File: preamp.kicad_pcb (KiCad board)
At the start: 2 copper layers, 49.5 x 43.2 mm, 46 parts, among them P1 CONN_01X04, P2 CONN_01X02, P3 CONN_01X04, P4 CONN_01X01, T1 TRANSFO2, U1 OPA137N, U2 LM7815CT, U3 LM7915CT, U4 OPA137N

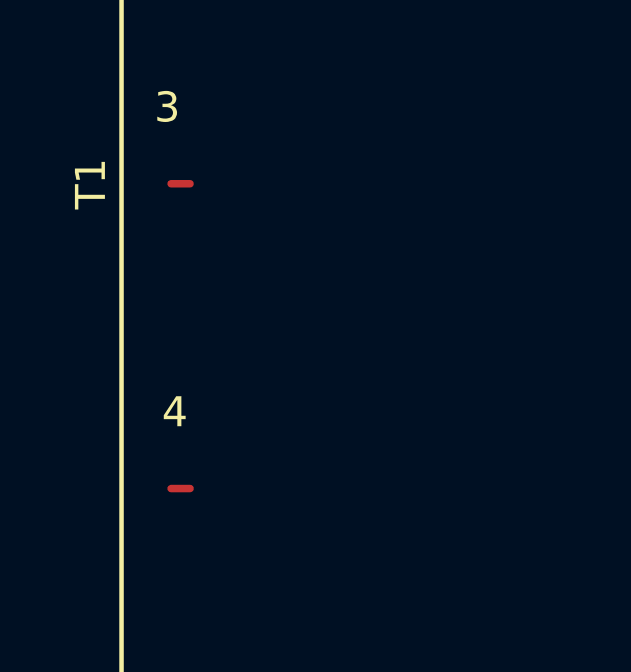
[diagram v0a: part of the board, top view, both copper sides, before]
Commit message: Clean up a couple of stray traces.
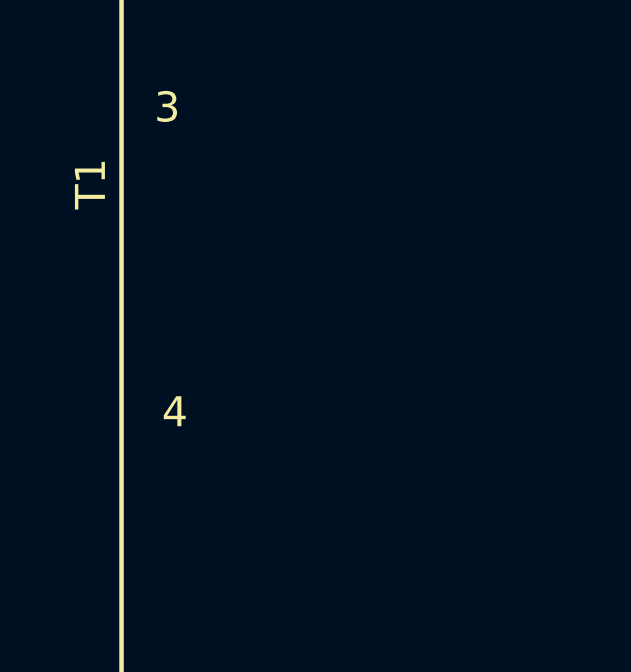
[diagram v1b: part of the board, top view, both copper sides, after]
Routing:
- net (no net): track 2.52 -> 1.25 mm
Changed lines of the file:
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@@
     (thickness 1.6)
     (drawings 9)
-    (tracks 232)
+    (tracks 230)
     (zones 0)
     (modules 46)
@@
   (page A4)
   (layers
-    (0 F.Cu signal hide)
+    (0 F.Cu signal)
     (31 B.Cu signal)
     (32 B.Adhes user)
@@
     (effects (font (size 0.5 0.5) (thickness 0.1)))
   )
-  (segment (start 42.038 78.74) (end 42.672 78.74) (width 0.25) (layer F.Cu) (net 0))
-  (segment (start 42.038 88.9) (end 42.672 88.9) (width 0.25) (layer F.Cu) (net 0))
   (segment (start 86.995 70.485) (end 87.138 70.628) (width 0.25) (layer F.Cu) (net 0))
   (segment (start 88.535 72.279) (end 88.535 71.755) (width 0.25) (layer F.Cu) (net 0) (status 30))

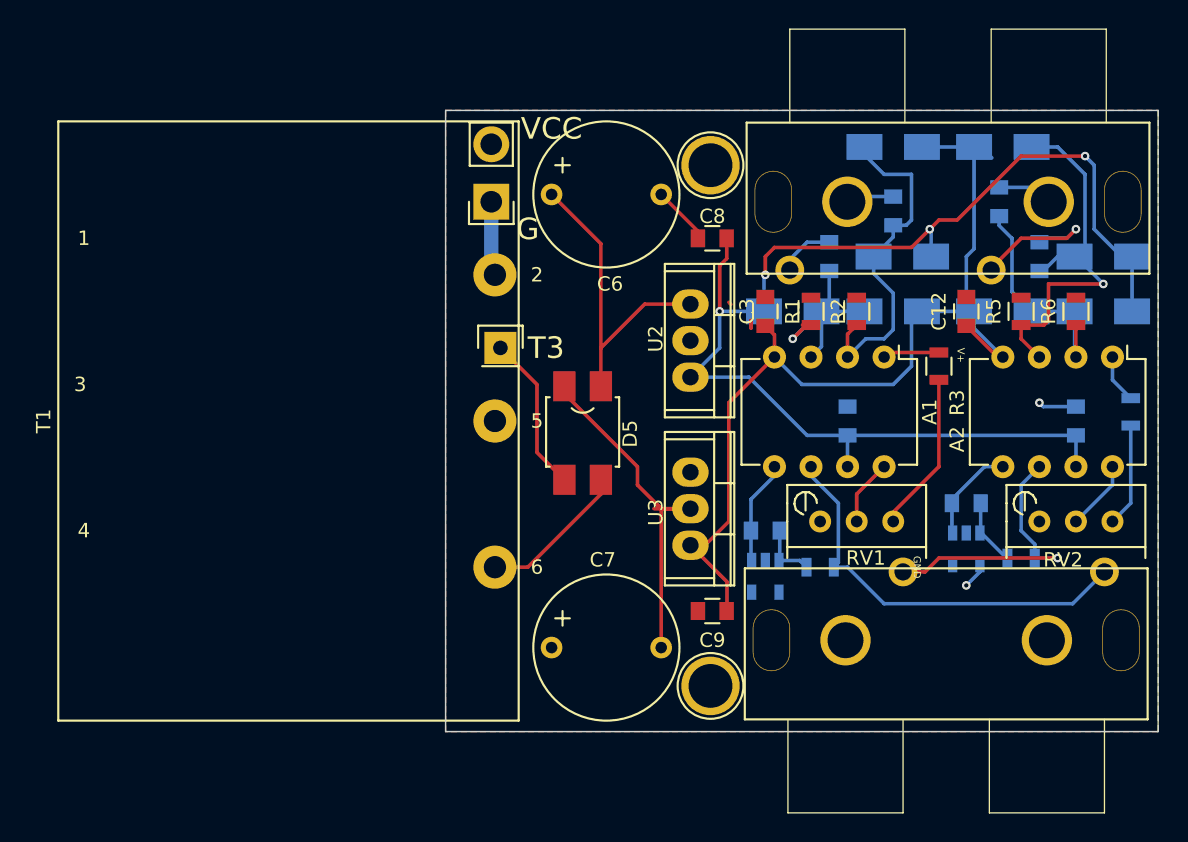
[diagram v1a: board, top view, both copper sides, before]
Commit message: Fix transformer value to adjust for RMS vs peak to peak voltage.  Add extra filtering caps at PSU output.  Fix the diode bridge pads.
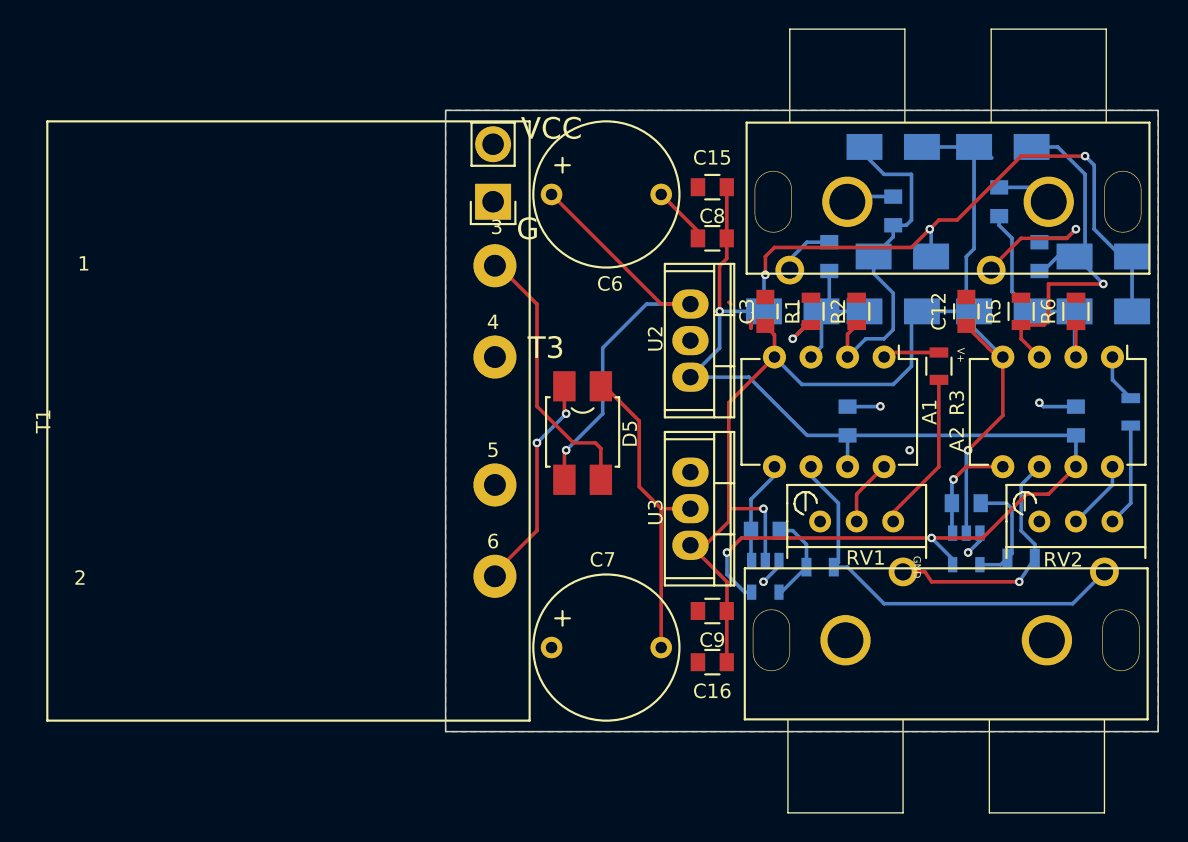
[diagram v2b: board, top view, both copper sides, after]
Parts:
- removed P4: CONN_01X01, Pin_Headers:Pin_Header_Straight_1x01
- removed REF** (x2): 1pin, Connect:1pin
- added C15: .1uf, Capacitors_SMD:C_0805, F.Cu at (85.9, 62.5)
- added C16: , Capacitors_SMD:C_0805, F.Cu at (85.9, 95.5)
- C9: value 1uF t -> 1uf t
- moved P2 0.13 mm to (70.6, 63.5)
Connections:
- U1 pad 2: Net-(U1-Pad2) -> -15V
- U1 pad 3: Net-(C4-Pad1) -> GND
- U1 pad 4: GND -> Net-(C4-Pad1)
- U1 pad 5: Net-(U1-Pad5) -> +15V
- U4 pad 2: Net-(U4-Pad2) -> -15V
- U4 pad 3: Net-(C13-Pad1) -> GND
- U4 pad 4: GND -> Net-(C13-Pad1)
- U4 pad 5: Net-(U4-Pad5) -> +15V
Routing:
- net +15V: track 92.0 -> 128.5 mm, vias 4 -> 6
- net -15V: track 68.2 -> 91.1 mm, vias 0 -> 2
- net Net-(D5-Pad4): track 11.0 -> 19.8 mm
- net Net-(C6-Pad1): track 23.0 -> 30.4 mm, vias 0 -> 1
- net Earth: track 5.69 -> 0.51 mm
- net Net-(D5-Pad2): track 11.3 -> 15.8 mm, vias 0 -> 2
- net GND: track 8.66 -> 12.8 mm, vias 2 -> 4
- net Net-(C7-Pad2): track 26.1 -> 22.1 mm
- net Net-(C13-Pad1): track 5.08 -> 8.53 mm
- net Net-(A2-Pad6): track 20.5 -> 18.2 mm
- net Net-(C4-Pad1): track 4.20 -> 6.47 mm
- net Net-(A2-Pad5): track 6.86 -> 7.88 mm, vias 0 -> 1
- net (no net): vias 0 -> 1

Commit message: Final ordered version on Oshpark.
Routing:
- net (no net): track 1.25 -> 0.20 mm
